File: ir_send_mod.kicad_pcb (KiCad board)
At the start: 2 copper layers, 50 x 50 mm, 29 parts, among them J1 Conn_01x03_Female, J2 Conn_01x05_Male, Q1 2N7000, Q2 IRF9024N, SW1 SW_Coded_SH-7040, SW2 SW_DIP_x04, SW3 SW_SPDT, SW4 SW_SPDT, U1 PIC12F629-IP

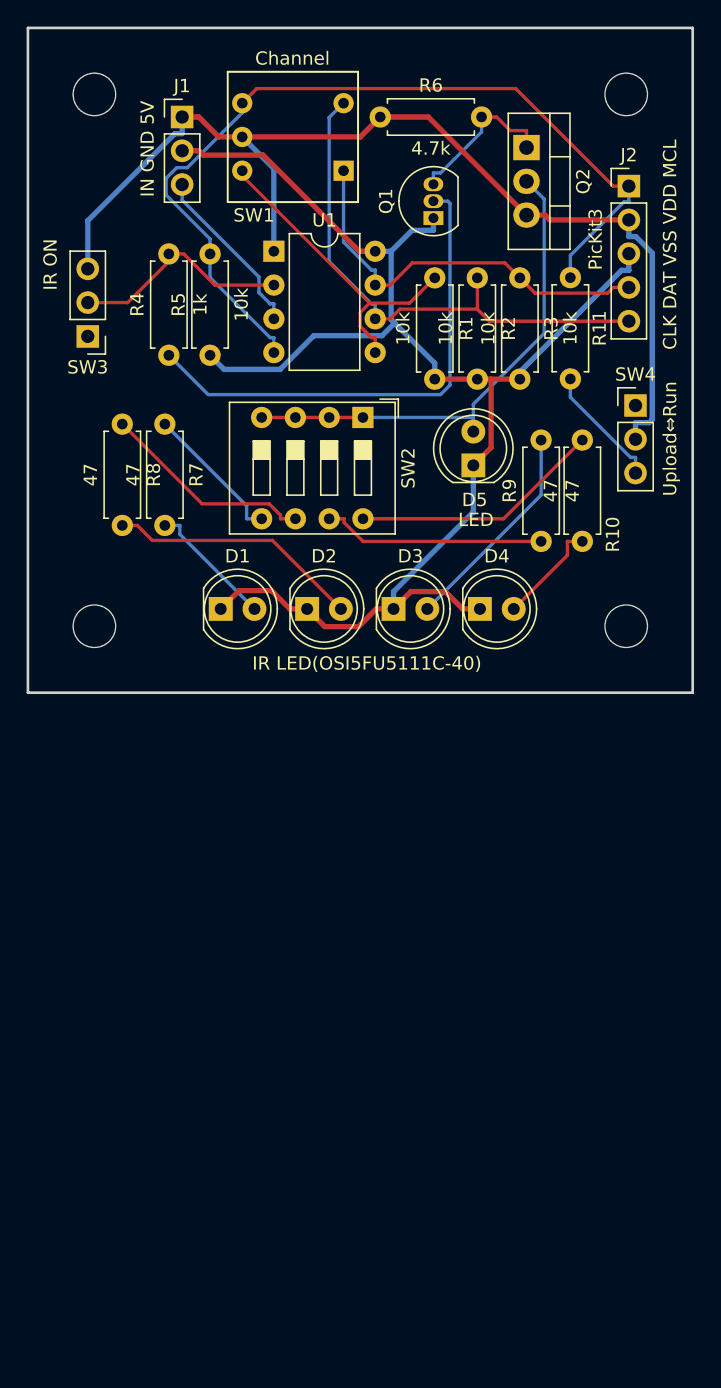
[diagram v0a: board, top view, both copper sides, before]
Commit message: Update: fix pcb size
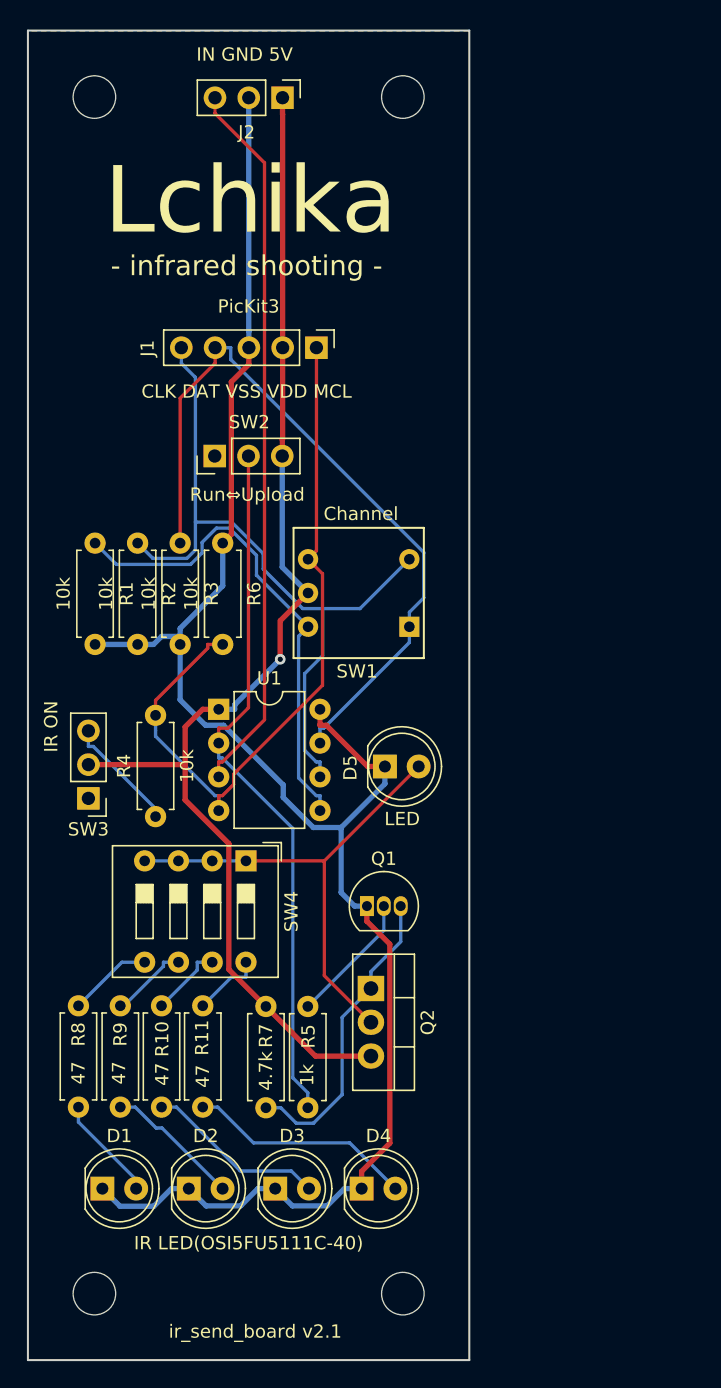
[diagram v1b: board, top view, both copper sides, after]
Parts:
- J1: value Conn_01x03_Female -> Conn_01x05_Male; footprint Connector_PinHeader_2.54mm:PinHeader_1x03_P2.54mm_Vertical -> Connector_PinHeader_2.54mm:PinHeader_1x05_P2.54mm_Vertical
- J2: value Conn_01x05_Male -> Conn_01x03_Female; footprint Connector_PinHeader_2.54mm:PinHeader_1x05_P2.54mm_Vertical -> Connector_PinHeader_2.54mm:PinHeader_1x03_P2.54mm_Vertical
- R11: value 10k -> 47
- R4: value 1k -> 10k
- R5: value 10k -> 1k
- R6: value 4.7k -> 10k
- R7: value 47 -> 4.7k
- SW2: value SW_DIP_x04 -> SW_SPDT; footprint Button_Switch_THT:SW_DIP_SPSTx04_Slide_9.78x12.34mm_W7.62mm_P2.54mm -> Connector_PinHeader_2.54mm:PinHeader_1x03_P2.54mm_Vertical
- SW4: value SW_SPDT -> SW_DIP_x04; footprint Connector_PinHeader_2.54mm:PinHeader_1x03_P2.54mm_Vertical -> Button_Switch_THT:SW_DIP_SPSTx04_Slide_9.78x12.34mm_W7.62mm_P2.54mm
- moved Q2 64.3 mm to (54.4, 116.8)
- moved R11 54.7 mm to (41.8, 118.0), turned to 270 degrees
- moved R10 53.0 mm to (38.6, 118.0)
- moved hole4 52.9 mm to (56.8, 139.7)
- moved Q1 52.0 mm to (54.1, 110.5), turned to 0 degrees
- moved hole3 50.2 mm to (33.6, 139.7)
- moved R5 49.5 mm to (49.6, 118.1), turned to 270 degrees
- moved R9 47.1 mm to (35.5, 118.0), turned to 270 degrees
- moved SW4 45.1 mm to (45.0, 107.2), turned to 270 degrees
- moved D1 44.5 mm to (34.2, 131.8)
- moved D2 44.5 mm to (40.7, 131.8)
- moved D3 44.5 mm to (47.2, 131.8)
- moved D4 44.5 mm to (53.7, 131.8)
- moved R7 44.5 mm to (46.5, 118.1)
- moved R8 43.9 mm to (32.4, 118.0)
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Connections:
- J1 pad 2: GND -> 5V
- J1 pad 3: Net-(J1-Pad3) -> GND
- J2 pad 1: Net-(J2-Pad1) -> 5V
- J2 pad 2: Net-(J1-Pad1) -> GND
- J2 pad 3: GND -> Net-(J2-Pad3)
- Q2 pad 3: Net-(J1-Pad1) -> 5V
- R10 pad 2: Net-(D4-Pad2) -> Net-(D3-Pad2)
- R11 pad 2: Net-(J2-Pad1) -> Net-(D4-Pad2)
- R2 pad 1: Net-(J2-Pad5) -> Net-(J1-Pad5)
- R3 pad 1: Net-(J2-Pad4) -> Net-(J1-Pad4)
- R4 pad 1: Net-(Q1-Pad2) -> Net-(R4-Pad1)
- R4 pad 2: Net-(R4-Pad2) -> Net-(J1-Pad1)
- R5 pad 1: GND -> Net-(Q1-Pad2)
- R5 pad 2: Net-(J2-Pad1) -> Net-(R5-Pad2)
- R6 pad 1: Net-(J1-Pad1) -> GND
- R6 pad 2: Net-(Q1-Pad3) -> Net-(J1-Pad1)
- R7 pad 1: Net-(R7-Pad1) -> 5V
- R7 pad 2: Net-(D1-Pad2) -> Net-(Q1-Pad3)
- R8 pad 2: Net-(D2-Pad2) -> Net-(D1-Pad2)
- R9 pad 2: Net-(D3-Pad2) -> Net-(D2-Pad2)
- SW1 pad 1: Net-(J2-Pad4) -> Net-(J1-Pad4)
- SW1 pad 2: Net-(J2-Pad5) -> Net-(J1-Pad5)
- SW1 pad 8: Net-(J2-Pad1) -> Net-(J1-Pad1)
- SW1 pad C: Net-(J1-Pad1) -> 5V
- SW2 pad 1: Net-(D5-Pad2) -> (no net)
- SW2 pad 2: Net-(D5-Pad2) -> Net-(R5-Pad2)
- SW2 pad 3: Net-(D5-Pad2) -> 5V
- SW3 pad 1: Net-(SW3-Pad1) -> (no net)
- SW3 pad 2: Net-(R4-Pad2) -> 5V
- SW3 pad 3: Net-(J1-Pad1) -> Net-(R4-Pad1)
- SW4 pad 1: Net-(SW4-Pad1) -> Net-(D5-Pad2)
- SW4 pad 2: Net-(J1-Pad1) -> Net-(D5-Pad2)
- SW4 pad 3: Net-(R11-Pad1) -> Net-(D5-Pad2)
- U1 pad 1: Net-(J1-Pad1) -> 5V
- U1 pad 2: Net-(R4-Pad2) -> Net-(R5-Pad2)
- U1 pad 3: Net-(J1-Pad3) -> Net-(J2-Pad3)
- U1 pad 4: Net-(J2-Pad1) -> Net-(J1-Pad1)
- U1 pad 6: Net-(J2-Pad5) -> Net-(J1-Pad5)
- U1 pad 7: Net-(J2-Pad4) -> Net-(J1-Pad4)
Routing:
- net 5V: track 0.00 -> 93.6 mm, vias 0 -> 1
- net Net-(J2-Pad1): track 66.6 -> 0.00 mm
- net Net-(J1-Pad4): track 0.00 -> 56.1 mm
- net Net-(J1-Pad5): track 0.00 -> 55.6 mm
- net Net-(J2-Pad3): track 0.00 -> 54.2 mm
- net Net-(R5-Pad2): track 0.00 -> 53.3 mm
- net Net-(J2-Pad5): track 40.4 -> 0.00 mm
- net Net-(J2-Pad4): track 30.6 -> 0.00 mm
- net Net-(Q1-Pad2): track 37.7 -> 9.92 mm
- net Net-(J1-Pad1): track 81.0 -> 56.3 mm
- net GND: track 113.1 -> 136.9 mm
- net Net-(R4-Pad2): track 17.0 -> 0.00 mm
- net Net-(R10-Pad1): track 19.0 -> 5.52 mm
- net Net-(J1-Pad3): track 13.1 -> 0.00 mm
- net Net-(R1-Pad1): track 24.3 -> 37.2 mm
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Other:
- board size 50 x 50 mm -> 33.2 x 100 mm
- board text added: "- infrared shooting -"
- board text added: "Lchika"
- board text added: "Run⇔Upload"
- board text added: "ir_send_board v2.1"
- board text removed: "Upload⇔Run"
- board text removed: "ir_send_board v1.1"
